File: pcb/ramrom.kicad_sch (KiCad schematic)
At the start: 18 parts, among them U11 HM628512, U12 HM628512, U13 HM628512, U14 HM628512, U15 HM628512, U16 HM628512, U17 HM628512, U18 HM628512, U21 W29C020

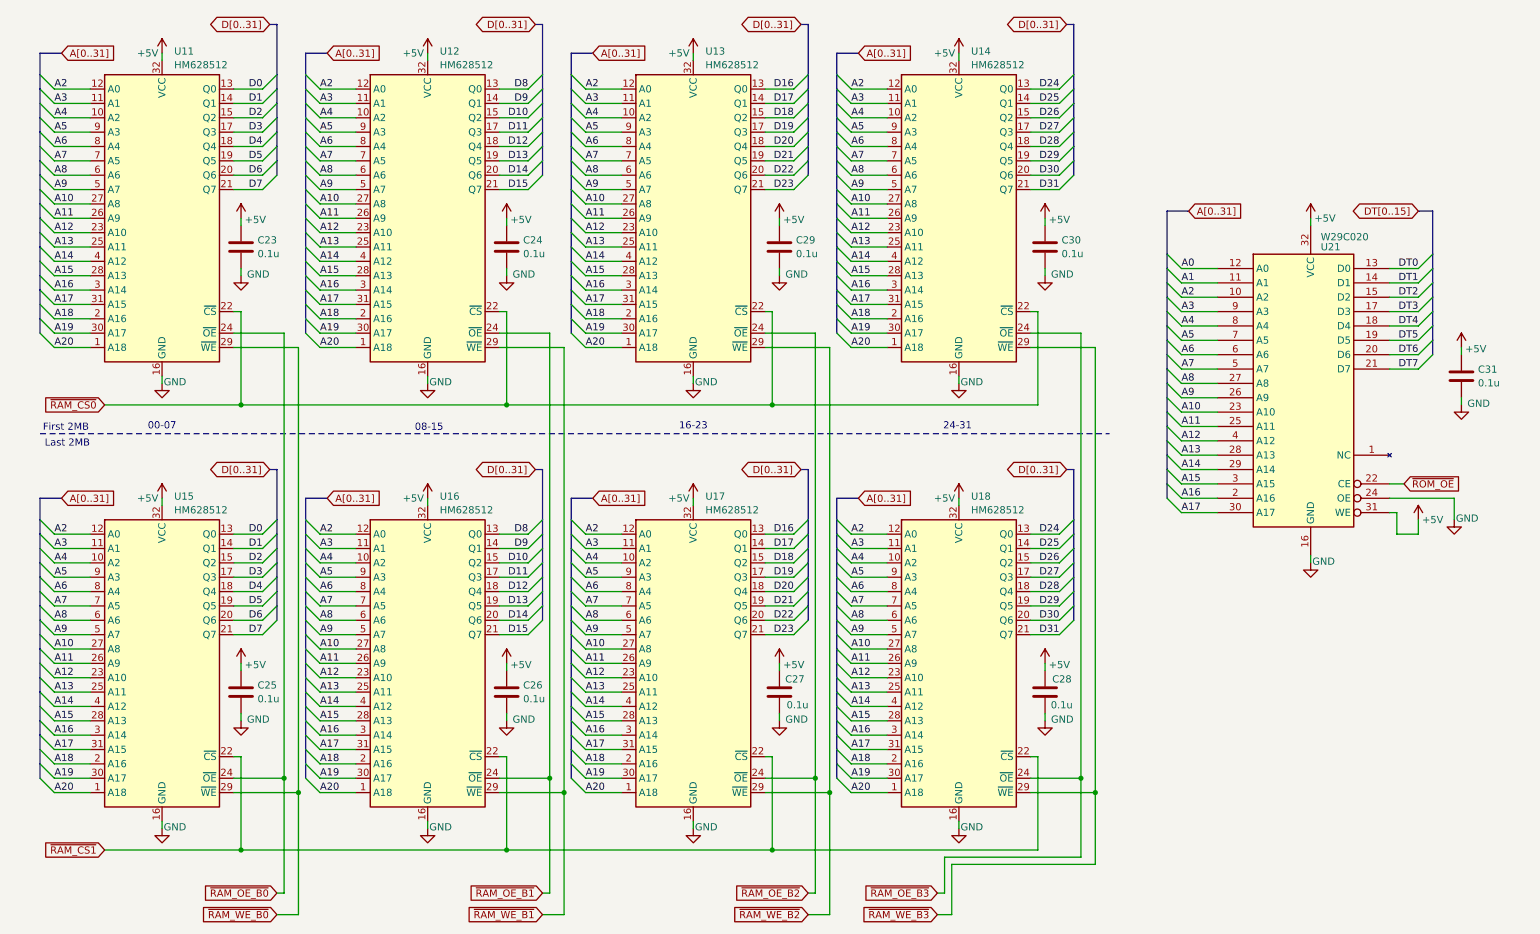
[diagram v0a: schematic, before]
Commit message: Add fpga sources, update schematic, update README
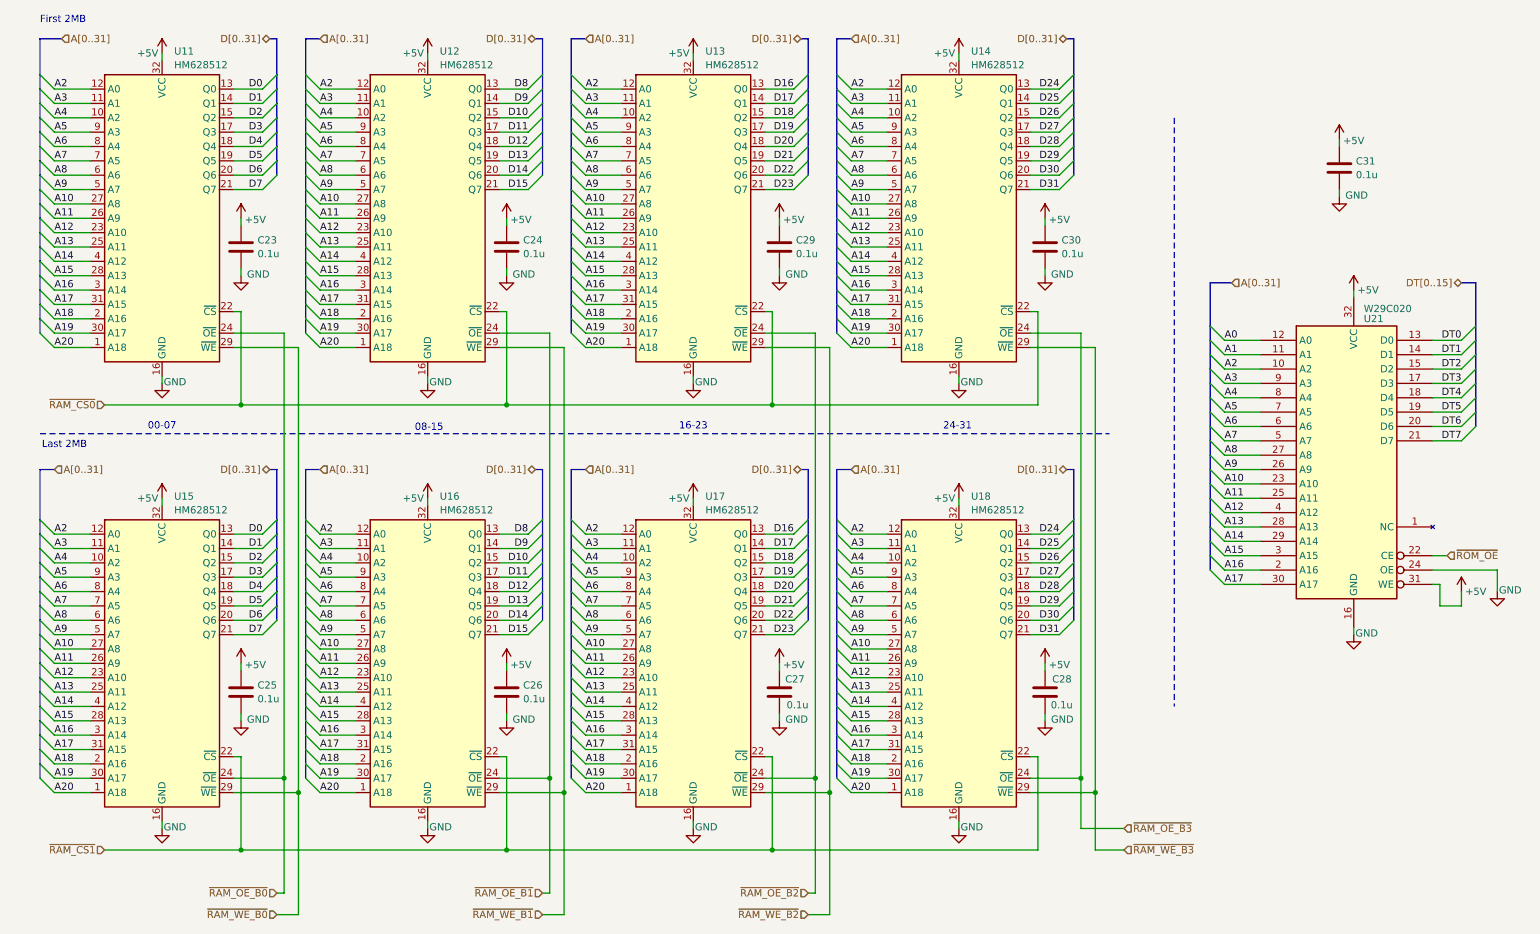
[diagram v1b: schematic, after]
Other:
- moved on the sheet: C31, U21
